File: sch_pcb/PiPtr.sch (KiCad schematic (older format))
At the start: 67 parts, among them J101 GLOBAL LINK 1 LEFT, J102 GLOBAL LINK 1 RIGHT, J104 GLOBAL LINK 2 LEFT, J106 GLOBAL LINK 2 RIGHT, J107 RASPBERRY_PI, J111 FP_PIXEL, J112 AM2302, J113 I2C1_5V, J114 I2C0_3v3, J117 OLED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

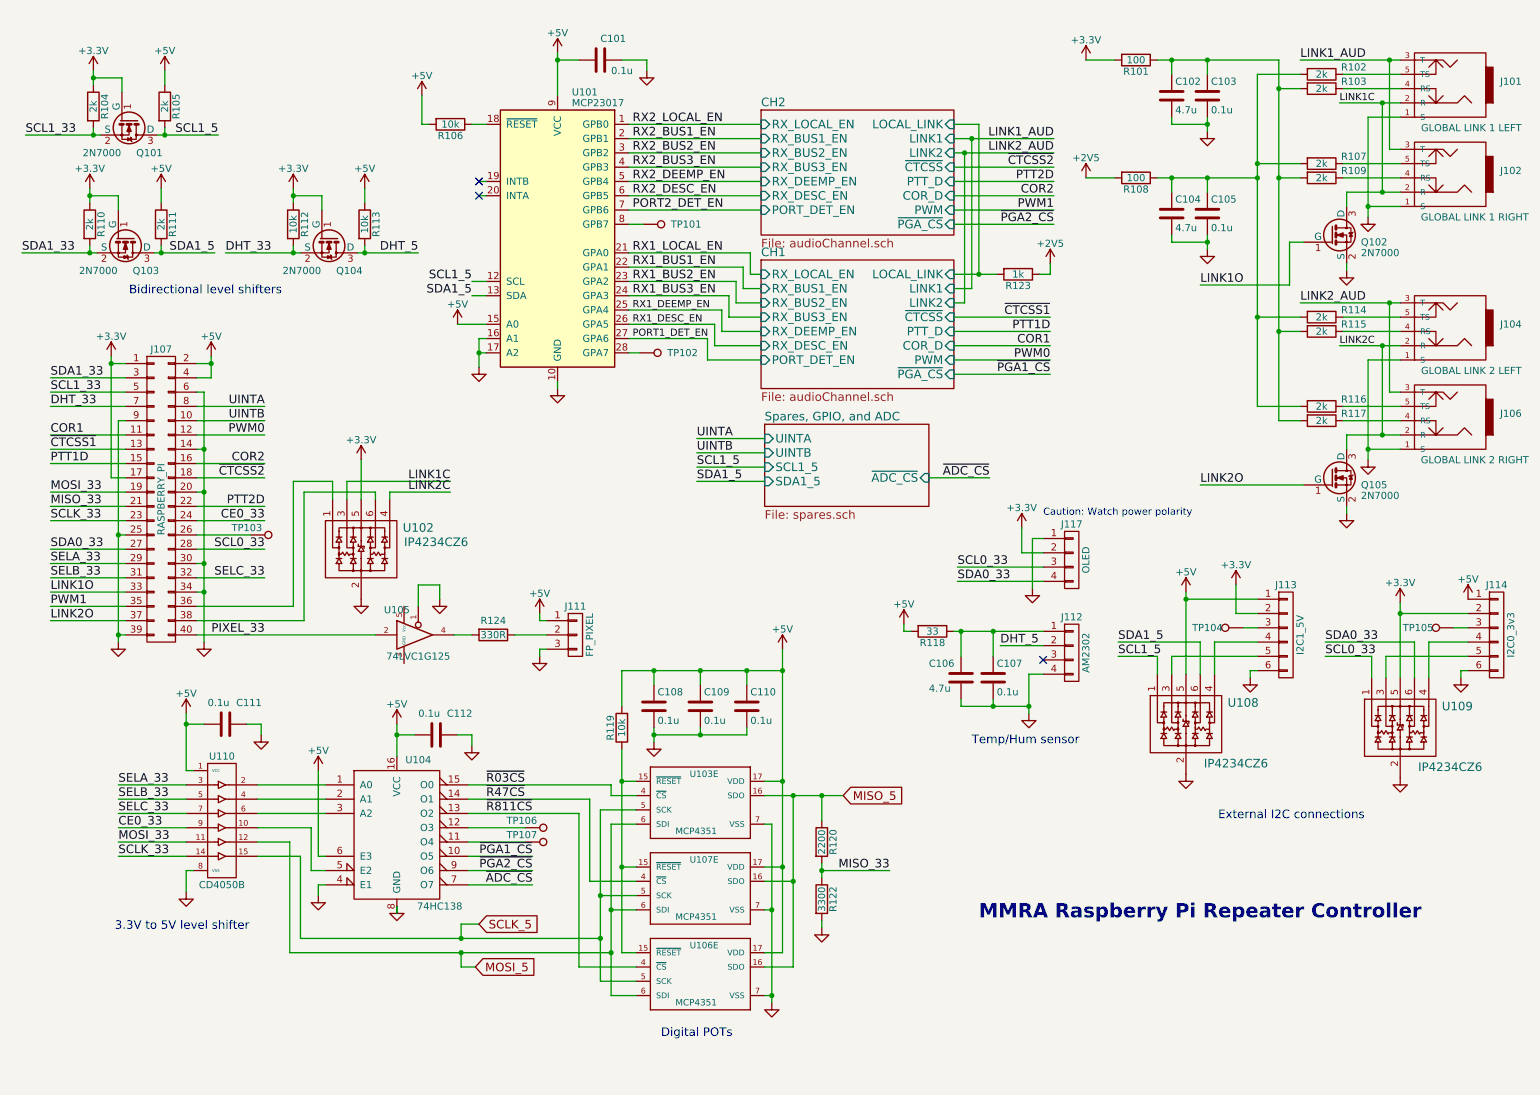
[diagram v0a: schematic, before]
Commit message: Updates based on emails
Disconnect SDO on PGAs
Add mounting holes 
More placement on PCB - for now, delete all 4xx sheet footprints.  Once channel 1 is placed, it will get copied to make channel 2.
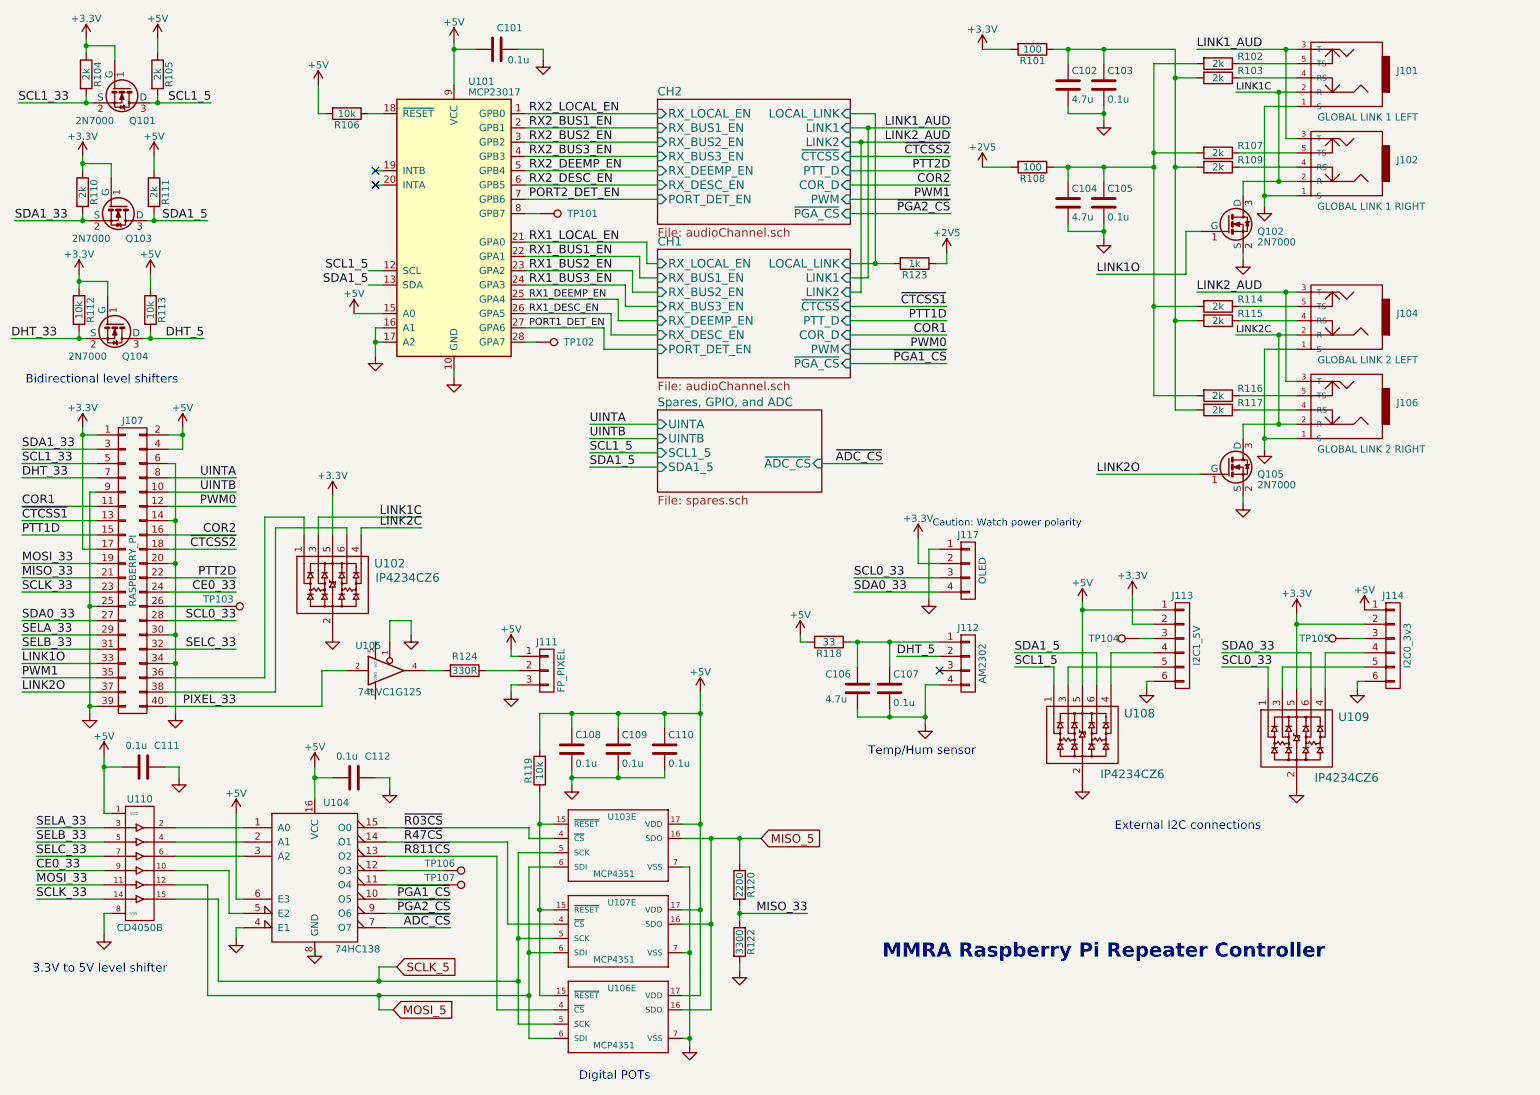
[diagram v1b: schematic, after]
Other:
- moved on the sheet: C101, C102, C103, C104, C105, C106, C107, C108, C109, C110, C111, C112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
